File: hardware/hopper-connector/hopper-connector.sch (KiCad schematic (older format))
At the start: 22 parts, among them P1 CONN_01X02, P2 CONN_01X02, P3 CONN_01X04, P4 CONN_01X04, P5 CONN_01X06, Q1 BC807-25, Q2 BTS430K2, U1 CNY17-3, U2 CNY17-3, U3 CNY17-3

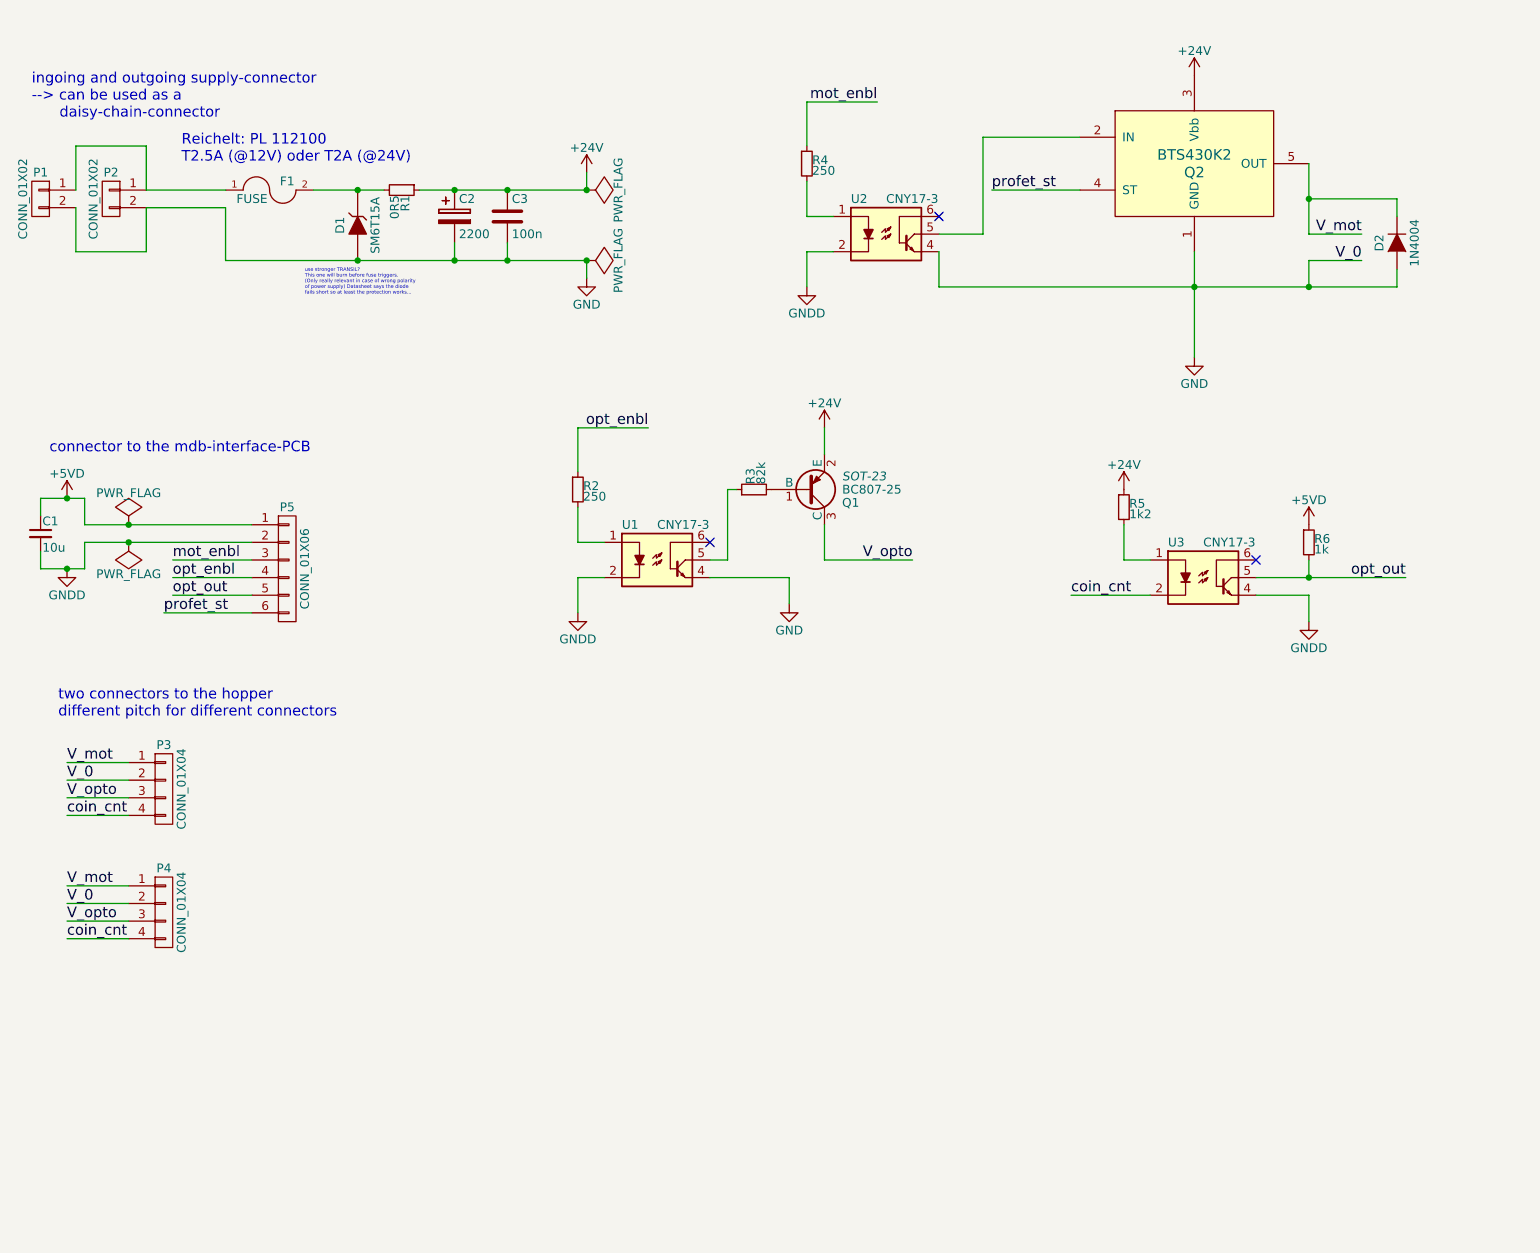
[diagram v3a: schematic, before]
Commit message: updated parts to be SMDable
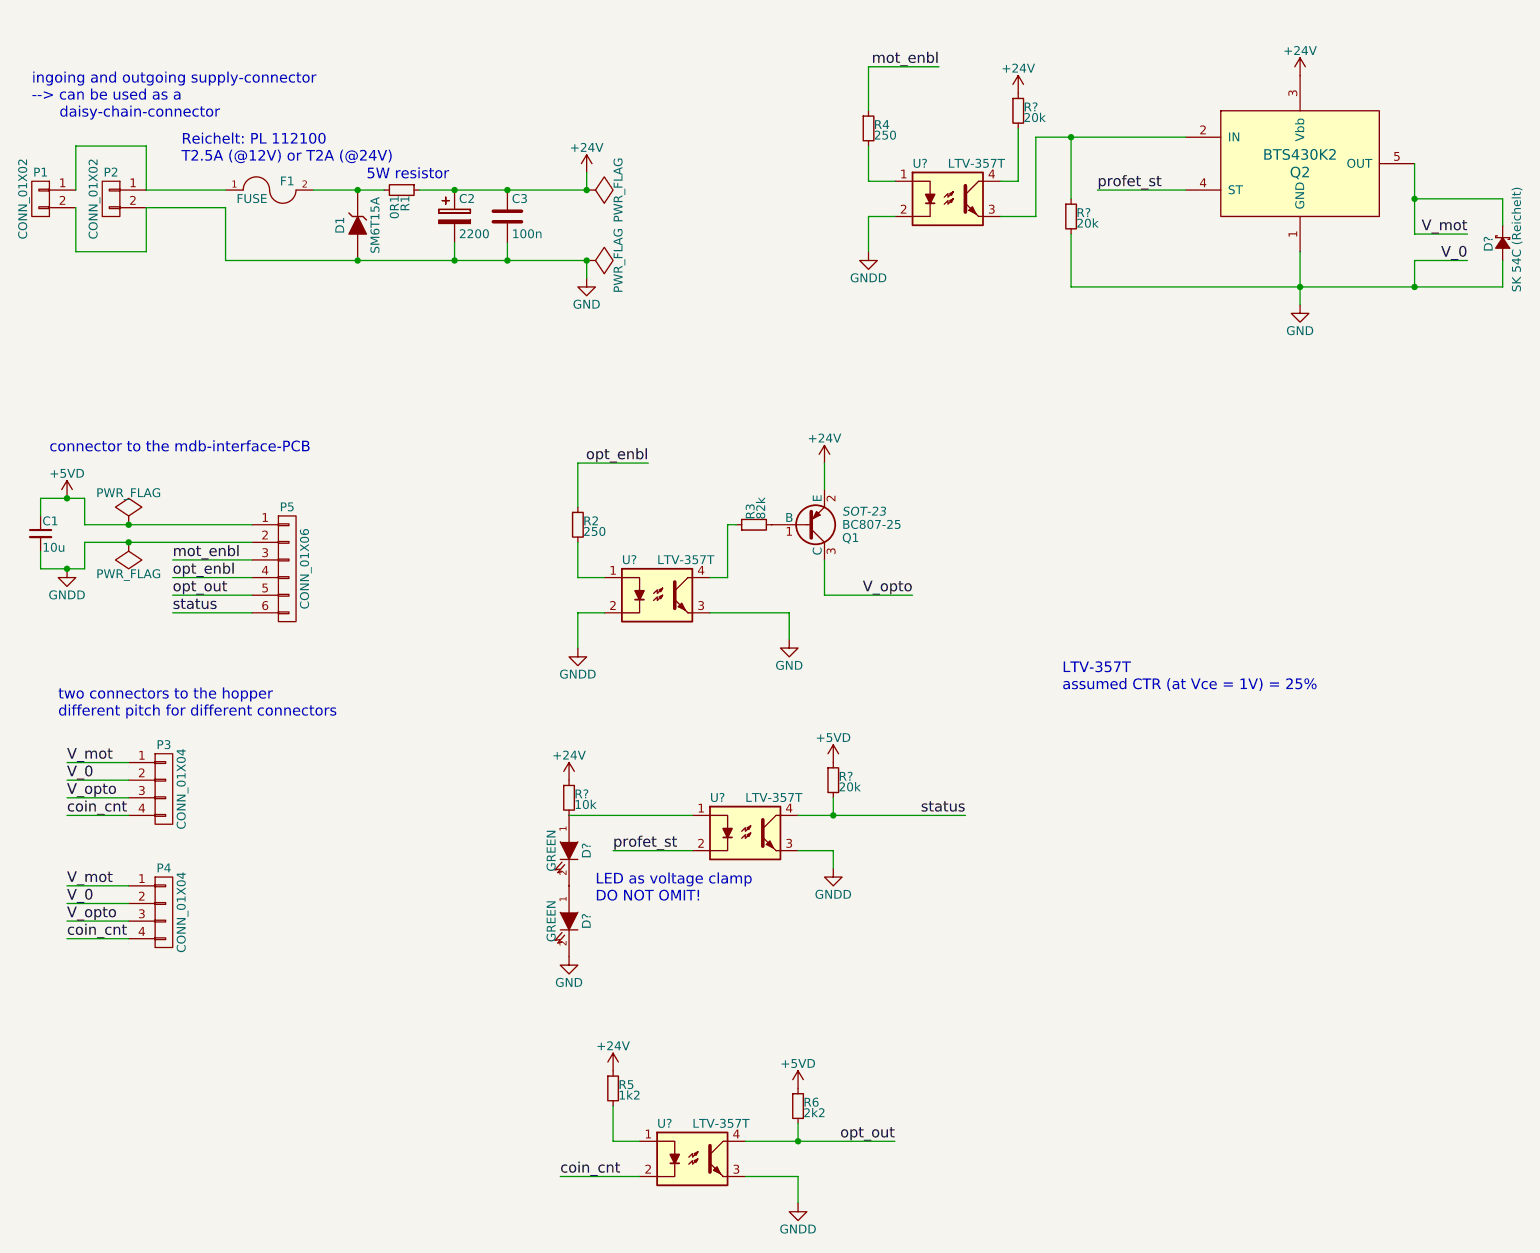
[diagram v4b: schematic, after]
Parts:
- removed D2: 1N4004, symbol D
- removed U1, U2, U3: CNY17-3, symbol CNY17-3
- added D?: SK 54C (Reichelt), symbol D_Schottky_Small
- added D? (x2): GREEN, symbol LED
- added R? (x3): 20k, symbol R_Small
- added R?: 10k, symbol R_Small
- added U? (x4): LTV-357T, Opto-Devices:Optocoupler_SMD_HandSoldering_KPC357_LTV35x_PC357_SingleChannel, symbol LTV-817
- R1: value 0R5 -> 0R1
- R6: value 1k -> 2k2
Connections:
- net +24V: now also R?.1, R?.1
- net +5VD: now also R?.1
- net GND: now also D?.1 (A), D?.2 (K), R?.2, U?.3
- net GNDD: now also U?.2, U?.2, U?.3, U?.3
- net V_mot: now also D?.2 (C)
- net coin_cnt: now also U?.2
- net opt_out: now also U?.4
- net profet_st: now also U?.2; no longer P5.6 (P6)
- net at R3.1: now also U?.4
- net at R4.2: now also U?.1
- net at Q2.2 (IN): now also R?.1, U?.3
- net at R2.2: now also U?.1
- net at R5.2: now also U?.1
- new net: R?.2, U?.4
- new net: D?.1 (A), R?.2, U?.1
- new net: D?.1 (A), D?.2 (K)
- new net status: P5.6 (P6), R?.2, U?.4
- no-connect marks 3 -> 0
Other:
- note added: "5W resistor"
- note added: "LED as voltage clamp\nDO NOT OMIT!"
- note added: "LTV-357T\nassumed CTR (at Vce = 1V) = 25%"
- note added: "Reichelt: PL 112100\nT2.5A (@12V) or T2A (@24V)"
- note removed: "Reichelt: PL 112100\nT2.5A (@12V) oder T2A (@24V)"
- note removed: "use stronger TRANSIL?\nThis one will burn before fuse triggers.\n(Only really relevant in case of wrong polarity\nof power supply) Datasheet says the diode\nfails short so at least the protection works..."
- moved on the sheet: Q1, Q2, R2, R3, R4, R5, R6

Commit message: annotation
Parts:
- P1, P2: value CONN_01X02 -> CONN_SUP
- P3: value CONN_01X04 -> CONN_HOPPER
- P4: value CONN_01X04 -> *
- P5: value CONN_01X06 -> CONN_PCB
- gave numbers to parts that had none: 11
- renumbered R2 to R3, R5 to R4, R3 to R5, R4 to R8
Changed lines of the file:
@@
 P 1400 4850
 F 0 "P3" H 1400 5100 50  0000 C CNN
-F 1 "CONN_01X04" V 1500 4850 50  0000 C CNN
+F 1 "CONN_HOPPER" V 1500 4850 50  0000 C CNN
 F 2 "" H 1400 4850 60  0000 C CNN
 F 3 "" H 1400 4850 60  0000 C CNN
@@
 P 1400 5550
 F 0 "P4" H 1400 5800 50  0000 C CNN
-F 1 "CONN_01X04" V 1500 5550 50  0000 C CNN
+F 1 "*" V 1500 5550 50  0000 C CNN
 F 2 "" H 1400 5550 60  0000 C CNN
 F 3 "" H 1400 5550 60  0000 C CNN
@@
 P 1100 1500
 F 0 "P2" H 1100 1650 50  0000 C CNN
-F 1 "CONN_01X02" V 1200 1500 50  0000 C CNN
+F 1 "CONN_SUP" V 1200 1500 50  0000 C CNN
 F 2 "" H 1100 1500 60  0000 C CNN
 F 3 "" H 1100 1500 60  0000 C CNN
@@
 P 700 1500
 F 0 "P1" H 700 1650 50  0000 C CNN
-F 1 "CONN_01X02" V 800 1500 50  0000 C CNN
+F 1 "CONN_SUP" V 800 1500 50  0000 C CNN
 F 2 "" H 700 1500 60  0000 C CNN
 F 3 "" H 700 1500 60  0000 C CNN
@@
 	5000 7050 5000 7200
 $Comp
-L R_Small R2
+L R_Small R3
 U 1 1 55468D1B
 P 3750 3350
-F 0 "R2" H 3780 3370 50  0000 L CNN
+F 0 "R3" H 3780 3370 50  0000 L CNN
 F 1 "250" H 3780 3310 50  0000 L CNN
 F 2 "" H 3750 3350 60  0000 C CNN
@@
 $EndComp
 $Comp
-L R_Small R4
+L R_Small R8
 U 1 1 55468EFB
 P 5400 1100
-F 0 "R4" H 5430 1120 50  0000 L CNN
+F 0 "R8" H 5430 1120 50  0000 L CNN
 F 1 "250" H 5430 1060 50  0000 L CNN
 F 2 "" H 5400 1100 60  0000 C CNN
@@
 $EndComp
 $Comp
-L R_Small R5
+L R_Small R4
 U 1 1 5546920A
 P 3950 6550
-F 0 "R5" H 3980 6570 50  0000 L CNN
+F 0 "R4" H 3980 6570 50  0000 L CNN
 F 1 "1k2" H 3980 6510 50  0000 L CNN
 F 2 "" H 3950 6550 60  0000 C CNN
@@
 $EndComp
 $Comp
-L R_Small R3
+L R_Small R5
 U 1 1 55466D39
 P 4750 3350
-F 0 "R3" H 4780 3370 50  0000 L CNN
+F 0 "R5" H 4780 3370 50  0000 L CNN
 F 1 "82k" H 4780 3310 50  0000 L CNN
 F 2 "" H 4750 3350 60  0000 C CNN
@@
 P 2100 3600
 F 0 "P5" H 2100 3950 50  0000 C CNN
-F 1 "CONN_01X06" V 2200 3600 50  0000 C CNN
+F 1 "CONN_PCB" V 2200 3600 50  0000 C CNN
 F 2 "" H 2100 3600 60  0000 C CNN
 F 3 "" H 2100 3600 60  0000 C CNN
@@
 status
 $Comp
-L R_Small R?
+L R_Small R9
 U 1 1 5548824D
 P 6250 1000
-F 0 "R?" H 6280 1020 50  0000 L CNN
+F 0 "R9" H 6280 1020 50  0000 L CNN
 F 1 "20k" H 6280 960 50  0000 L CNN
 F 2 "" H 6250 1000 60  0000 C CNN
@@
 $EndComp
 $Comp
-L R_Small R?
+L R_Small R10
 U 1 1 55488281
 P 6550 1600
-F 0 "R?" H 6580 1620 50  0000 L CNN
+F 0 "R10" H 6580 1620 50  0000 L CNN
 F 1 "20k" H 6580 1560 50  0000 L CNN
 F 2 "" H 6550 1600 60  0000 C CNN
@@
 $EndComp
 $Comp
-L +24V #PWR?
+L +24V #PWR018
 U 1 1 554882C1
 P 6250 900
-F 0 "#PWR?" H 6250 750 50  0001 C CNN
+F 0 "#PWR018" H 6250 750 50  0001 C CNN
 F 1 "+24V" H 6250 1040 50  0000 C CNN
 F 2 "" H 6250 900 60  0000 C CNN
@@
 	7850 1800 7850 2100
 $Comp
-L D_Schottky_Small D?
+L D_Schottky_Small D4
 U 1 1 5548A865
 P 9000 1750
-F 0 "D?" H 8950 1830 50  0000 L CNN
+F 0 "D4" H 8950 1830 50  0000 L CNN
 F 1 "SK 54C (Reichelt)" H 8720 1670 50  0000 L CNN
 F 2 "" V 9000 1750 60  0000 C CNN
@@
 $EndComp
 $Comp
-L LTV-817 U?
+L LTV-817 U4
 U 1 1 5548B70A
 P 5850 1500
-F 0 "U?" H 5650 1700 50  0000 L CNN
+F 0 "U4" H 5650 1700 50  0000 L CNN
 F 1 "LTV-357T" H 5850 1700 50  0000 L CNN
 F 2 "Opto-Devices:Optocoupler_SMD_HandSoldering_KPC357_LTV35x_PC357_SingleChannel" H 5650 1300 50  0001 L CIN
@@
 	6250 1400 6250 1100
 $Comp
-L LTV-817 U?
+L LTV-817 U1
 U 1 1 5548BAC6
 P 4200 3750
-F 0 "U?" H 4000 3950 50  0000 L CNN
+F 0 "U1" H 4000 3950 50  0000 L CNN
 F 1 "LTV-357T" H 4200 3950 50  0000 L CNN
 F 2 "Opto-Devices:Optocoupler_SMD_HandSoldering_KPC357_LTV35x_PC357_SingleChannel" H 4000 3550 50  0001 L CIN
@@
 $EndComp
 $Comp
-L LTV-817 U?
+L LTV-817 U2
 U 1 1 5548C560
 P 4400 6950
-F 0 "U?" H 4200 7150 50  0000 L CNN
+F 0 "U2" H 4200 7150 50  0000 L CNN
 F 1 "LTV-357T" H 4400 7150 50  0000 L CNN
 F 2 "Opto-Devices:Optocoupler_SMD_HandSoldering_KPC357_LTV35x_PC357_SingleChannel" H 4200 6750 50  0001 L CIN
@@
 profet_st
 $Comp
-L LTV-817 U?
+L LTV-817 U3
 U 1 1 5548C883
 P 4700 5100
-F 0 "U?" H 4500 5300 50  0000 L CNN
+F 0 "U3" H 4500 5300 50  0000 L CNN
 F 1 "LTV-357T" H 4700 5300 50  0000 L CNN
 F 2 "Opto-Devices:Optocoupler_SMD_HandSoldering_KPC357_LTV35x_PC357_SingleChannel" H 4500 4900 50  0001 L CIN
@@
 	3950 5200 4400 5200
 $Comp
-L R_Small R?
+L R_Small R2
 U 1 1 5548D1D1
 P 3700 4900
-F 0 "R?" H 3730 4920 50  0000 L CNN
+F 0 "R2" H 3730 4920 50  0000 L CNN
 F 1 "10k" H 3730 4860 50  0000 L CNN
 F 2 "" H 3700 4900 60  0000 C CNN
@@
 $EndComp
 $Comp
-L GND #PWR?
+L GND #PWR019
 U 1 1 5548D21A
 P 3700 5800
-F 0 "#PWR?" H 3700 5550 50  0001 C CNN
+F 0 "#PWR019" H 3700 5550 50  0001 C CNN
 F 1 "GND" H 3700 5650 50  0000 C CNN
 F 2 "" H 3700 5800 60  0000 C CNN
@@
 $EndComp
 $Comp
-L +24V #PWR?
+L +24V #PWR020
 U 1 1 5548D276
 P 3700 4800
-F 0 "#PWR?" H 3700 4650 50  0001 C CNN
+F 0 "#PWR020" H 3700 4650 50  0001 C CNN
 F 1 "+24V" H 3700 4940 50  0000 C CNN
 F 2 "" H 3700 4800 60  0000 C CNN
@@
 	4400 5000 3700 5000
 $Comp
-L GNDD #PWR?
+L GNDD #PWR021
 U 1 1 5548D7B7
 P 5200 5300
-F 0 "#PWR?" H 5200 5050 50  0001 C CNN
+F 0 "#PWR021" H 5200 5050 50  0001 C CNN
 F 1 "GNDD" H 5200 5150 50  0000 C CNN
 F 2 "" H 5200 5300 60  0000 C CNN
@@
 	5200 5200 5200 5300
 $Comp
-L +5VD #PWR?
+L +5VD #PWR022
 U 1 1 5548D950
 P 5200 4700
-F 0 "#PWR?" H 5200 4550 50  0001 C CNN
+F 0 "#PWR022" H 5200 4550 50  0001 C CNN
 F 1 "+5VD" H 5200 4840 50  0000 C CNN
 F 2 "" H 5200 4700 60  0000 C CNN
@@
 $EndComp
 $Comp
-L R_Small R?
+L R_Small R7
 U 1 1 5548D9E2
 P 5200 4800
-F 0 "R?" H 5230 4820 50  0000 L CNN
+F 0 "R7" H 5230 4820 50  0000 L CNN
 F 1 "20k" H 5230 4760 50  0000 L CNN
 F 2 "" H 5200 4800 60  0000 C CNN
@@
 status
 $Comp
-L LED D?
+L LED D2
 U 1 1 5548E810
 P 3700 5200
-F 0 "D?" H 3700 5300 50  0000 C CNN
+F 0 "D2" H 3700 5300 50  0000 C CNN
 F 1 "GREEN" H 3700 5100 50  0000 C CNN
 F 2 "" H 3700 5200 60  0000 C CNN
@@
 $EndComp
 $Comp
-L LED D?
+L LED D3
 U 1 1 5548E999
 P 3700 5600
-F 0 "D?" H 3700 5700 50  0000 C CNN
+F 0 "D3" H 3700 5700 50  0000 C CNN
 F 1 "GREEN" H 3700 5500 50  0000 C CNN
 F 2 "" H 3700 5600 60  0000 C CNN

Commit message: added notice on how to connect to MDB-interface
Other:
- note added: "connect\nPin 1-2 to 5V-BAK-connector\nPin 3-4 to K1\nPin 5-6 to K2\n"
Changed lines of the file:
@@
 Text Notes 2550 1400 0    60   ~ 0
 5W resistor
+Text Notes 2250 3700 0    60   ~ 0
+connect\nPin 1-2 to 5V-BAK-connector\nPin 3-4 to K1\nPin 5-6 to K2\n
 $EndSCHEMATC

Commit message: fixed some issues with schematic
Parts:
- C2: value 2200 -> 2200u
- D1: value SM6T15A -> P6SMB 33A SMD
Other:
- note added: "TODO: This LED gets fried (P=.5W)"
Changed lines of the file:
@@
 P 2500 1650
 F 0 "D1" H 2500 1750 50  0000 C CNN
-F 1 "SM6T15A" H 2500 1550 50  0000 C CNN
+F 1 "P6SMB 33A SMD" H 2350 1550 50  0000 C CNN
 F 2 "" H 2500 1650 60  0000 C CNN
 F 3 "" H 2500 1650 60  0000 C CNN
@@
 P 3050 1600
 F 0 "C2" H 3075 1700 50  0000 L CNN
-F 1 "2200" H 3075 1500 50  0000 L CNN
+F 1 "2200u" H 3075 1500 50  0000 L CNN
 F 2 "" H 3088 1450 30  0000 C CNN
 F 3 "" H 3050 1600 60  0000 C CNN
@@
 Text Notes 2250 3700 0    60   ~ 0
 connect\nPin 1-2 to 5V-BAK-connector\nPin 3-4 to K1\nPin 5-6 to K2\n
+Text Notes 2300 6550 0    60   ~ 0
+TODO: This LED gets fried (P=.5W)
 $EndSCHEMATC

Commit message: minor fixes in schematic for Reichelt-order
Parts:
- removed P1, P2: CONN_SUP, symbol CONN_01X02
- added P? (x2): CONN_SUP, symbol CONN_01X04
- R4: value 1k2 -> 1k2, P=.5W
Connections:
- net GND: now also P?.3 (P3), P?.3 (P3), P?.4 (P4), P?.4 (P4)
- net at F1.1: now also P?.1 (P1), P?.1 (P1), P?.2 (P2), P?.2 (P2)
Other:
- note removed: "TODO: This LED gets fried (P=.5W)"
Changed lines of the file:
@@
 Text Label 850  5700 0    60   ~ 0
 coin_cnt
-$Comp
-L CONN_01X02 P2
-U 1 1 5544CE5E
-P 1100 1500
-F 0 "P2" H 1100 1650 50  0000 C CNN
-F 1 "CONN_SUP" V 1200 1500 50  0000 C CNN
-F 2 "" H 1100 1500 60  0000 C CNN
-F 3 "" H 1100 1500 60  0000 C CNN
-	1    1100 1500
-	-1   0    0    -1
-$EndComp
-$Comp
-L CONN_01X02 P1
-U 1 1 5544CF50
-P 700 1500
-F 0 "P1" H 700 1650 50  0000 C CNN
-F 1 "CONN_SUP" V 800 1500 50  0000 C CNN
-F 2 "" H 700 1500 60  0000 C CNN
-F 3 "" H 700 1500 60  0000 C CNN
-	1    700  1500
-	-1   0    0    -1
-$EndComp
 Text Notes 650  1050 0    60   ~ 0
 ingoing and outgoing supply-connector\n--> can be used as a\n      daisy-chain-connector
@@
 P 3950 6550
 F 0 "R4" H 3980 6570 50  0000 L CNN
-F 1 "1k2" H 3980 6510 50  0000 L CNN
+F 1 "1k2, P=.5W" H 3980 6510 50  0000 L CNN
 F 2 "" H 3950 6550 60  0000 C CNN
 F 3 "" H 3950 6550 60  0000 C CNN
@@
 Wire Wire Line
 	8500 1300 8500 1700
-Wire Wire Line
-	900  1450 900  1200
-Wire Wire Line
-	900  1200 1300 1200
-Wire Wire Line
-	1300 1200 1300 1450
-Wire Wire Line
-	900  1550 900  1800
-Wire Wire Line
-	900  1800 1300 1800
-Wire Wire Line
-	1300 1800 1300 1550
-Wire Wire Line
-	1300 1450 1750 1450
-Wire Wire Line
-	1300 1550 1750 1550
 $Comp
 L FUSE F1
@@
 Connection ~ 3050 1450
 Wire Wire Line
-	1750 1550 1750 1850
-Wire Wire Line
-	1750 1850 3800 1850
+	1600 1850 3800 1850
 Wire Wire Line
 	3050 1850 3050 1750
@@
 Text Notes 2250 3700 0    60   ~ 0
 connect\nPin 1-2 to 5V-BAK-connector\nPin 3-4 to K1\nPin 5-6 to K2\n
-Text Notes 2300 6550 0    60   ~ 0
-TODO: This LED gets fried (P=.5W)
+$Comp
+L CONN_01X04 P?
+U 1 1 557EEB97
+P 750 1650
+F 0 "P?" H 750 1900 50  0000 C CNN
+F 1 "CONN_SUP" V 850 1650 50  0000 C CNN
+F 2 "" H 750 1650 60  0000 C CNN
+F 3 "" H 750 1650 60  0000 C CNN
+	1    750  1650
+	-1   0    0    -1
+$EndComp
+$Comp
+L CONN_01X04 P?
+U 1 1 557EEBE6
+P 1200 1650
+F 0 "P?" H 1200 1900 50  0000 C CNN
+F 1 "CONN_SUP" V 1300 1650 50  0000 C CNN
+F 2 "" H 1200 1650 60  0000 C CNN
+F 3 "" H 1200 1650 60  0000 C CNN
+	1    1200 1650
+	-1   0    0    -1
+$EndComp
+Wire Wire Line
+	950  1350 950  1600
+Wire Wire Line
+	950  1700 950  1950
+Wire Wire Line
+	1400 1350 1400 1600
+Wire Wire Line
+	1400 1700 1400 1950
+Wire Wire Line
+	1400 1950 950  1950
+Connection ~ 1400 1800
+Connection ~ 950  1800
+Wire Wire Line
+	1600 1850 1600 1800
+Wire Wire Line
+	1600 1800 1400 1800
+Wire Wire Line
+	950  1350 1400 1350
+Connection ~ 1400 1500
+Connection ~ 950  1500
+Wire Wire Line
+	1750 1450 1600 1450
+Wire Wire Line
+	1600 1450 1600 1500
+Wire Wire Line
+	1600 1500 1400 1500
 $EndSCHEMATC
